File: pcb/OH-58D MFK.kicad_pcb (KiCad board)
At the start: 2 copper layers, 114.5 x 140 mm, 123 parts, among them J1 Conn_01x07_Pin, J2 Conn_01x10_Pin, J3 Conn_01x03_Pin, J4 Conn_01x02_Pin, J5 Conn_01x02_Pin, SW1 SW_Push, SW10 SW_Push, SW11 SW_Push, SW12 SW_Push, SW13 SW_Push, SW14 SW_Push, SW15 SW_Push, SW16 SW_Push, SW17 SW_Push, SW18 SW_Push, SW19 SW_Push, SW2 SW_Push, SW20 SW_Push, SW21 SW_Push, SW22 SW_Push, SW23 SW_Push, SW24 SW_Push, SW25 SW_Push, SW26 SW_Push, SW27 SW_Push, SW28 SW_Push, SW29 SW_Push, SW3 SW_Push, SW30 SW_Push, SW31 SW_Push, SW32 SW_Push, SW33 SW_Push, SW34 SW_Push, SW35 SW_Push, SW36 SW_Push, SW37 SW_Push, SW38 SW_Push, SW39 SW_Push, SW4 SW_Push, SW40 SW_Push, SW41 SW_Push, SW42 SW_Push, SW43 SW_Push, SW44 SW_Push, SW45 SW_Push, SW46 SW_Push, SW47 SW_Push, SW5 SW_Push, SW6 SW_Push, SW7 SW_Push, SW8 SW_Push, SW9 SW_Push

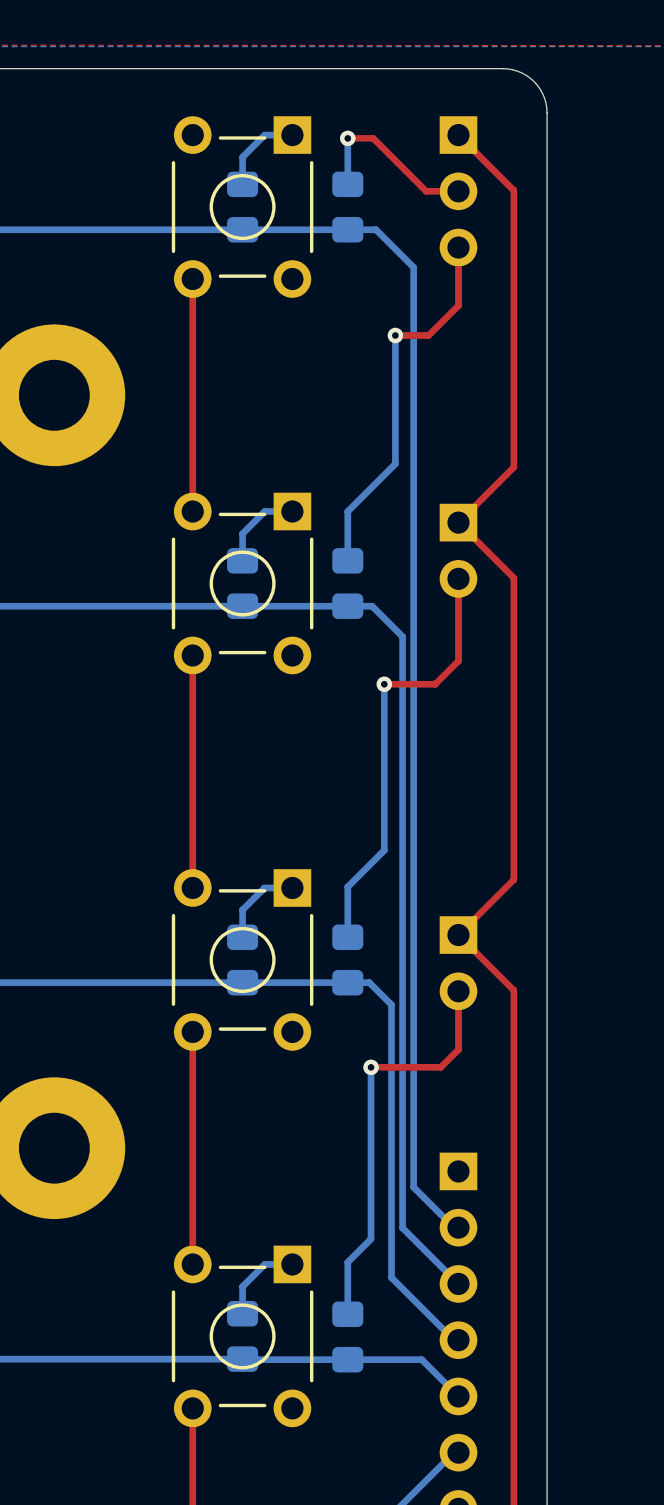
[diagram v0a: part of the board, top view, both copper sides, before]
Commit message: Move diodes to get more clearance to pads
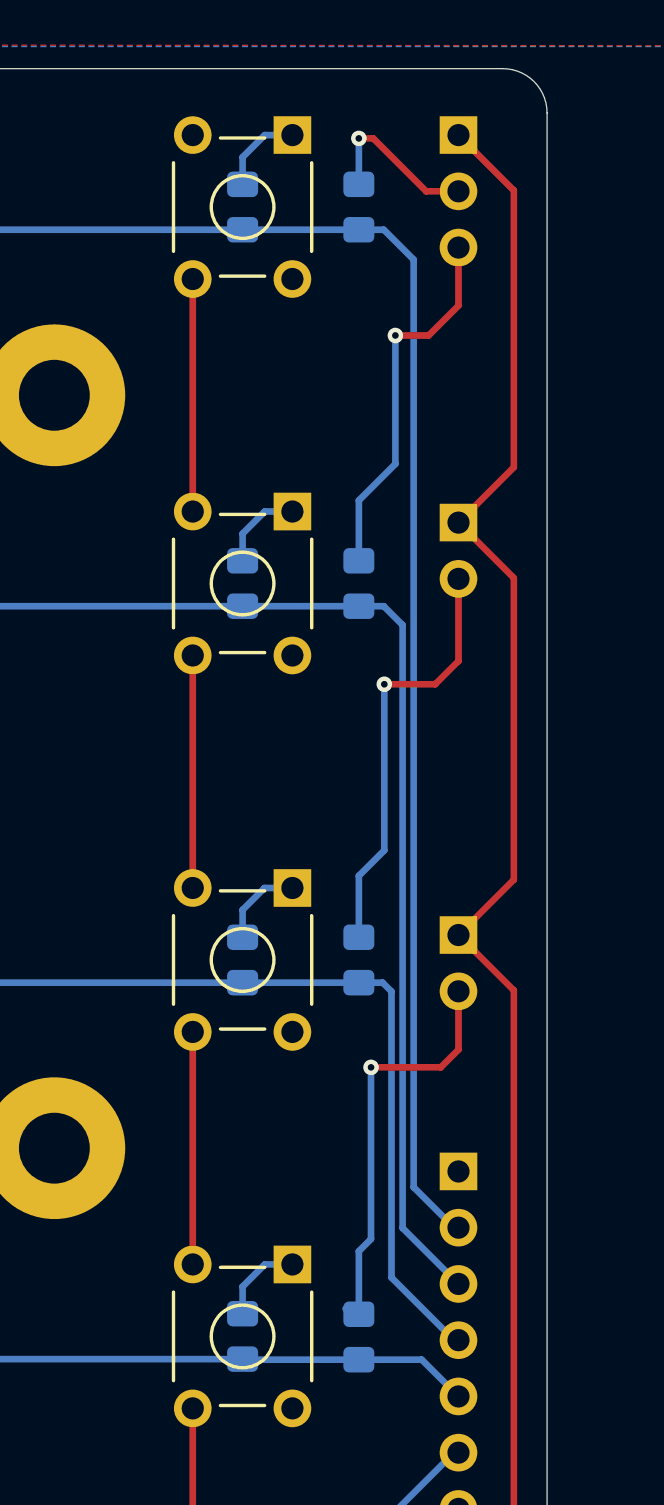
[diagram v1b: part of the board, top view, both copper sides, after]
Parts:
- moved D48 0.50 mm to (100.2, 41.0)
- moved D49 0.50 mm to (100.2, 58.0)
- moved D50 0.50 mm to (100.2, 75.0)
- moved D51 0.50 mm to (100.2, 92.0)
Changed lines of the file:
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@@
 	(footprint "Diode_SMD:D_0805_2012Metric_Pad1.15x1.40mm_HandSolder"
 		(layer "B.Cu")
-		(at 99.65 41.025 90)
+		(at 100.15 41.025 90)
 		(descr "Diode SMD 0805 (2012 Metric), square (rectangular) end terminal, IPC_7351 nominal, (Body size source: https://docs.google.com/spreadsheets/d/1BsfQQcO9C6DZCsRaXUlFlo91Tg2WpOkGARC1WS5S8t0/edit?usp=sharing), generated with kicad-footprint-generator")
 		(tags "diode handsolder")
@@
 	(footprint "Diode_SMD:D_0805_2012Metric_Pad1.15x1.40mm_HandSolder"
 		(layer "B.Cu")
-		(at 99.65 75.025 90)
+		(at 100.15 75.025 90)
 		(descr "Diode SMD 0805 (2012 Metric), square (rectangular) end terminal, IPC_7351 nominal, (Body size source: https://docs.google.com/spreadsheets/d/1BsfQQcO9C6DZCsRaXUlFlo91Tg2WpOkGARC1WS5S8t0/edit?usp=sharing), generated with kicad-footprint-generator")
 		(tags "diode handsolder")
@@
 	(footprint "Diode_SMD:D_0805_2012Metric_Pad1.15x1.40mm_HandSolder"
 		(layer "B.Cu")
-		(at 99.65 92.05 90)
+		(at 100.15 92.05 90)
 		(descr "Diode SMD 0805 (2012 Metric), square (rectangular) end terminal, IPC_7351 nominal, (Body size source: https://docs.google.com/spreadsheets/d/1BsfQQcO9C6DZCsRaXUlFlo91Tg2WpOkGARC1WS5S8t0/edit?usp=sharing), generated with kicad-footprint-generator")
 		(tags "diode handsolder")
@@
 	(footprint "Diode_SMD:D_0805_2012Metric_Pad1.15x1.40mm_HandSolder"
 		(layer "B.Cu")
-		(at 99.65 58.025 90)
+		(at 100.15 58.025 90)
 		(descr "Diode SMD 0805 (2012 Metric), square (rectangular) end terminal, IPC_7351 nominal, (Body size source: https://docs.google.com/spreadsheets/d/1BsfQQcO9C6DZCsRaXUlFlo91Tg2WpOkGARC1WS5S8t0/edit?usp=sharing), generated with kicad-footprint-generator")
 		(tags "diode handsolder")
@@
 	)
 	(segment
-		(start 43.9 42.05)
-		(end 52.4 42.05)
+		(start 101.275 42.05)
+		(end 102.625 43.4)
 		(width 0.3)
 		(layer "B.Cu")
@@
 	)
 	(segment
-		(start 102.625 43.75)
-		(end 102.625 85.29)
+		(start 100.15 42.05)
+		(end 101.275 42.05)
 		(width 0.3)
 		(layer "B.Cu")
@@
 	)
 	(segment
-		(start 77.9 42.05)
-		(end 94.9 42.05)
+		(start 94.9 42.05)
+		(end 94.975 41.975)
 		(width 0.3)
 		(layer "B.Cu")
@@
 	(segment
 		(start 94.9 42.05)
-		(end 99.65 42.05)
+		(end 100.15 42.05)
 		(width 0.3)
 		(layer "B.Cu")
@@
 	)
 	(segment
-		(start 100.925 42.05)
-		(end 102.625 43.75)
+		(start 43.9 42.05)
+		(end 52.4 42.05)
+		(width 0.3)
+		(layer "B.Cu")
+		(net 2)
+	)
+	(segment
+		(start 102.625 43.4)
+		(end 102.625 85.29)
 		(width 0.3)
 		(layer "B.Cu")
@@
 	)
 	(segment
-		(start 60.9 42.05)
-		(end 77.9 42.05)
+		(start 77.9 42.05)
+		(end 94.9 42.05)
 		(width 0.3)
 		(layer "B.Cu")
@@
 	)
 	(segment
-		(start 52.4 42.05)
-		(end 60.9 42.05)
+		(start 60.9 42.05)
+		(end 77.9 42.05)
 		(width 0.3)
 		(layer "B.Cu")
@@
 	)
 	(segment
-		(start 99.65 42.05)
-		(end 100.925 42.05)
+		(start 52.4 42.05)
+		(end 60.9 42.05)
 		(width 0.3)
 		(layer "B.Cu")
@@
 	)
 	(segment
-		(start 60.8 59.425)
-		(end 60.9 59.325)
+		(start 94.9 59.05)
+		(end 101.275 59.05)
 		(width 0.3)
 		(layer "B.Cu")
@@
 	)
 	(segment
-		(start 100.75 59.05)
-		(end 102.125 60.425)
+		(start 60.8 59.425)
+		(end 60.9 59.325)
 		(width 0.3)
 		(layer "B.Cu")
@@
 	)
 	(segment
-		(start 99.65 59.05)
-		(end 100.75 59.05)
-		(width 0.3)
-		(layer "B.Cu")
-		(net 6)
-	)
-	(segment
-		(start 94.9 59.05)
-		(end 99.65 59.05)
+		(start 60.9 59.05)
+		(end 77.9 59.05)
 		(width 0.3)
 		(layer "B.Cu")
@@
 	)
 	(segment
-		(start 60.9 59.05)
-		(end 77.9 59.05)
+		(start 94.7 59.325)
+		(end 94.8 59.425)
 		(width 0.3)
 		(layer "B.Cu")
@@
 	)
 	(segment
-		(start 94.7 59.325)
-		(end 94.8 59.425)
+		(start 101.275 59.05)
+		(end 102.125 59.9)
 		(width 0.3)
 		(layer "B.Cu")
@@
 	)
 	(segment
-		(start 102.125 60.425)
+		(start 102.125 59.9)
 		(end 102.125 87.13)
 		(width 0.3)
@@
 	)
 	(segment
-		(start 43.9 76.05)
-		(end 52.4 76.05)
-		(width 0.3)
-		(layer "B.Cu")
-		(net 11)
-	)
-	(segment
-		(start 101.625 77.05)
-		(end 100.625 76.05)
+		(start 101.625 89.37)
+		(end 104.45 92.195)
 		(width 0.3)
 		(layer "B.Cu")
@@
 	)
 	(segment
-		(start 101.625 77.05)
-		(end 101.625 89.37)
+		(start 43.9 76.05)
+		(end 52.4 76.05)
 		(width 0.3)
 		(layer "B.Cu")
@@
 	(segment
 		(start 94.9 76.05)
-		(end 99.65 76.05)
+		(end 101.225 76.05)
 		(width 0.3)
 		(layer "B.Cu")
@@
 	)
 	(segment
-		(start 100.625 76.05)
-		(end 99.65 76.05)
+		(start 60.9 76.05)
+		(end 77.9 76.05)
 		(width 0.3)
 		(layer "B.Cu")
@@
 	)
 	(segment
-		(start 60.9 76.05)
-		(end 77.9 76.05)
+		(start 52.4 76.05)
+		(end 60.9 76.05)
 		(width 0.3)
 		(layer "B.Cu")
@@
 	)
 	(segment
-		(start 52.4 76.05)
-		(end 60.9 76.05)
+		(start 101.625 76.45)
+		(end 101.625 89.37)
 		(width 0.3)
 		(layer "B.Cu")
@@
 	)
 	(segment
-		(start 101.625 89.37)
-		(end 104.45 92.195)
+		(start 101.225 76.05)
+		(end 101.625 76.45)
 		(width 0.3)
 		(layer "B.Cu")
@@
 	)
 	(segment
-		(start 99.65 93.075)
-		(end 102.99 93.075)
-		(width 0.3)
-		(layer "B.Cu")
-		(net 16)
-	)
-	(segment
 		(start 43.9 93.05)
 		(end 52.4 93.05)
@@
 	)
 	(segment
-		(start 77.9 93.05)
-		(end 94.9 93.05)
+		(start 94.925 93.075)
+		(end 102.99 93.075)
 		(width 0.3)
 		(layer "B.Cu")
@@
 	)
 	(segment
-		(start 60.9 93.05)
-		(end 77.9 93.05)
+		(start 102.99 93.075)
+		(end 104.465 94.55)
 		(width 0.3)
 		(layer "B.Cu")
@@
 	)
 	(segment
-		(start 95.175 93.05)
-		(end 95.2 93.075)
+		(start 77.9 93.05)
+		(end 94.9 93.05)
 		(width 0.3)
 		(layer "B.Cu")
@@
 	)
 	(segment
-		(start 94.9 93.05)
-		(end 95.175 93.05)
+		(start 60.9 93.05)
+		(end 77.9 93.05)
 		(width 0.3)
 		(layer "B.Cu")
@@
 	)
 	(segment
-		(start 95.2 93.075)
-		(end 99.65 93.075)
+		(start 94.9 93.05)
+		(end 94.925 93.075)
 		(width 0.3)
 		(layer "B.Cu")
@@
 	)
 	(segment
-		(start 102.99 93.075)
-		(end 104.465 94.55)
-		(width 0.3)
-		(layer "B.Cu")
-		(net 16)
-	)
-	(segment
 		(start 44.9 88.775)
 		(end 46.15 88.775)
@@
 	)
 	(segment
-		(start 104.65 40.315)
-		(end 103.19 40.315)
+		(start 103.19 40.315)
+		(end 100.8 37.925)
 		(width 0.3)
 		(layer "F.Cu")
@@
 	)
 	(segment
-		(start 103.19 40.315)
-		(end 100.8 37.925)
+		(start 100.8 37.925)
+		(end 100.15 37.925)
 		(width 0.3)
 		(layer "F.Cu")
@@
 	)
 	(segment
-		(start 100.8 37.925)
-		(end 99.75 37.925)
+		(start 104.65 40.315)
+		(end 103.19 40.315)
 		(width 0.3)
 		(layer "F.Cu")
@@
 	)
 	(via
-		(at 99.65 37.925)
+		(at 100.15 37.925)
 		(size 0.7)
 		(drill 0.3)
@@
 	)
 	(segment
-		(start 99.65 39.775)
-		(end 99.65 37.925)
+		(start 100.15 40)
+		(end 100.15 37.925)
 		(width 0.3)
 		(layer "B.Cu")
@@
 	)
 	(segment
-		(start 99.65 54.775)
-		(end 101.8 52.625)
+		(start 101.8 52.625)
+		(end 101.8 46.825)
 		(width 0.3)
 		(layer "B.Cu")
@@
 	)
 	(segment
-		(start 99.65 56.775)
-		(end 99.65 54.775)
+		(start 100.15 57)
+		(end 100.15 54.275)
 		(width 0.3)
 		(layer "B.Cu")
@@
 	)
 	(segment
-		(start 101.8 52.625)
-		(end 101.8 46.825)
+		(start 100.15 54.275)
+		(end 101.8 52.625)
 		(width 0.3)
 		(layer "B.Cu")
@@
 	)
 	(segment
-		(start 101.3 62.575)
+		(start 100.15 71.225)
 		(end 101.3 70.075)
 		(width 0.3)
@@
 	)
 	(segment
-		(start 99.65 73.775)
-		(end 99.65 71.725)
+		(start 101.3 70.075)
+		(end 101.3 62.575)
 		(width 0.3)
 		(layer "B.Cu")
@@
 	)
 	(segment
-		(start 101.3 70.075)
-		(end 99.65 71.725)
+		(start 100.15 74)
+		(end 100.15 71.225)
 		(width 0.3)
 		(layer "B.Cu")
@@
 	)
 	(segment
-		(start 100.7 87.625)
-		(end 99.65 88.675)
+		(start 100.15 88.175)
+		(end 100.15 91.025)
 		(width 0.3)
 		(layer "B.Cu")
@@
 	)
 	(segment
-		(start 99.65 88.675)
-		(end 99.65 90.775)
+		(start 100.7 87.625)
+		(end 100.15 88.175)
 		(width 0.3)
 		(layer "B.Cu")
